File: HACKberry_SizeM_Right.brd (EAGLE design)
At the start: 50.9 x 56.6 mm, 14 parts, among them IC1 OKI-78SR-5_1.5-W36H-C

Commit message: rev1.1
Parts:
- moved U$7 5.24 mm to (44.5, 11.4), turned to 270 degrees
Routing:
- net GND: track 166.2 -> 128.4 mm, vias 0 -> 2
- net SWITCH_HOLD: track 85.2 -> 56.4 mm, vias 3 -> 2
- net +5V: track 59.0 -> 49.9 mm
- net PIN_MIDDLESERVO: track 62.0 -> 69.7 mm, vias 1 -> 2
- net PIN_INDEXSERVO: track 66.4 -> 74.0 mm, vias 3 -> 0
- net V+: track 25.4 -> 32.5 mm, vias 0 -> 1
- net PIN_THUMBSERVO: track 56.9 -> 63.2 mm, vias 3 -> 2
- net N$11: track 58.1 -> 55.2 mm, vias 1 -> 2
- net SWITCH_INIT: track 52.4 -> 53.3 mm, vias 3 -> 2
- net SWITCH_THUMB: track 28.9 -> 29.6 mm, vias 1 -> 2
- net SWITCH_MODE: track 40.5 -> 39.9 mm, vias 3 -> 2
- net N$1: vias 0 -> 1
- added copper zone on layer 1, net GND
- removed copper zone on layer 1, net N$4
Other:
- outline, holes or cut-outs redrawn

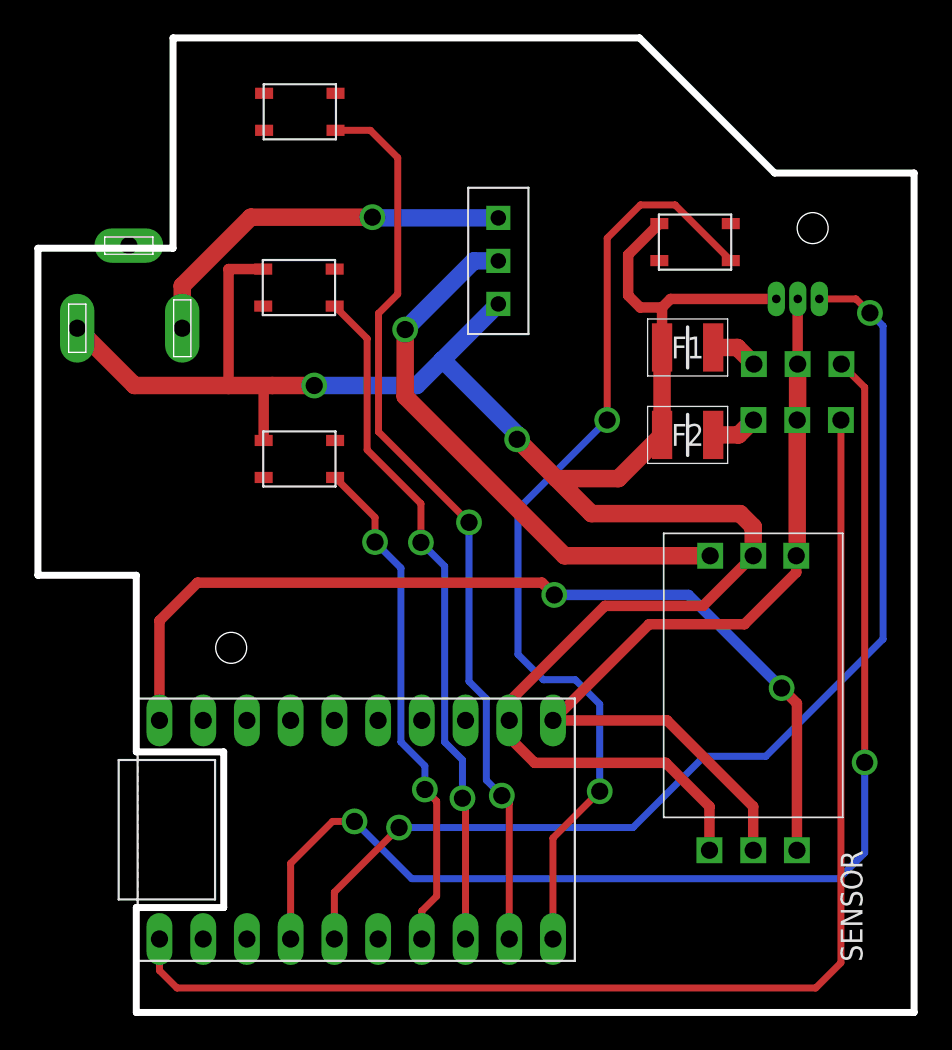
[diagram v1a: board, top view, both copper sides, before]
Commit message: ポリスイッチを取り除き, サーボの電源ラインにパスコンを追加した.
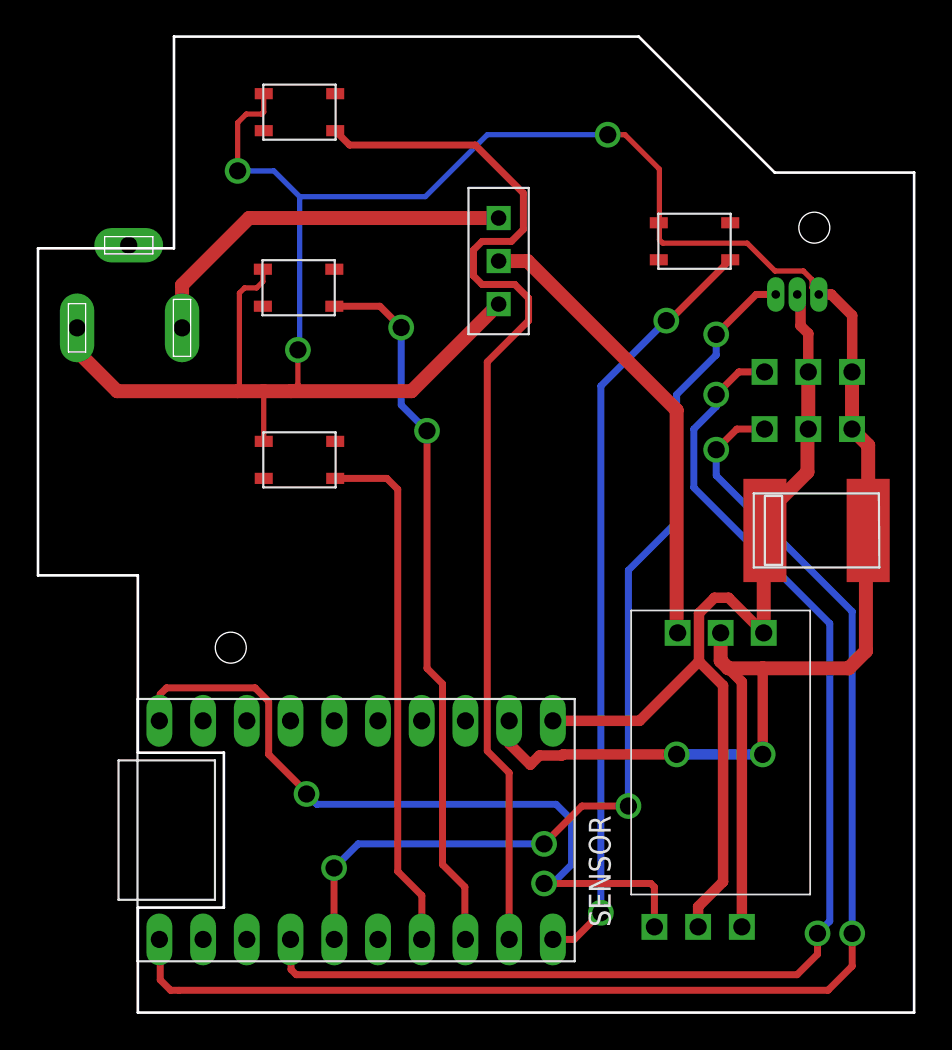
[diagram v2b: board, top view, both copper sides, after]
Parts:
- removed F1, F2: MICROSMD010F-2, HbHandBoard_SizeM:FUSC3226X85N
- added U$8: P-11867_ECASD41C476M040KA0, Akizuki:ECASD41C476M040KA0
- moved U$7 5.48 mm to (41.2, 6.98), turned to 90 degrees
- moved IC1 4.86 mm to (42.6, 17.1)
- moved INDEXPIN 0.83 mm to (47.6, 35.9), turned to 270 degrees
- moved MIDDLEPIN 0.77 mm to (47.6, 39.2), turned to 270 degrees
- moved THUMBPIN 0.26 mm to (47.0, 43.7), turned to 270 degrees
- moved U$5 0.06 mm to (41.0, 46.8)
- moved U$4 0.05 mm to (18.1, 34.1)
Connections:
- removed net N$2: F1.2, MIDDLEPIN.SERVO_GND
- removed net N$3: F2.2, INDEXPIN.SERVO_GND
- net +5V: now also U$8.+
- net GND: now also INDEXPIN.SERVO_GND, MIDDLEPIN.SERVO_GND, U$8.-; no longer F1.1, F2.1
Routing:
- net GND: track 128.4 -> 170.3 mm, vias 2 -> 5
- net SWITCH_HOLD: track 56.4 -> 44.6 mm
- net N$11: track 55.2 -> 44.1 mm
- net SWITCH_INIT: track 53.3 -> 61.9 mm, vias 2 -> 0
- net PIN_THUMBSERVO: track 63.2 -> 56.7 mm, vias 2 -> 4
- net PIN_INDEXSERVO: track 74.0 -> 80.0 mm, vias 0 -> 2
- net V+: track 32.5 -> 26.9 mm, vias 1 -> 0
- net +5V: track 49.9 -> 55.3 mm
- net PIN_MIDDLESERVO: track 69.7 -> 72.9 mm
- net N$2: track 2.77 -> 0.00 mm
- net N$3: track 2.70 -> 0.00 mm
- net SWITCH_MODE: track 39.9 -> 41.5 mm
- net SWITCH_THUMB: track 29.6 -> 30.6 mm, vias 2 -> 0
- net N$1: vias 1 -> 0
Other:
- board size 50.9 x 56.6 mm -> 50.9 x 56.7 mm

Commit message: 8milのDRUに対応
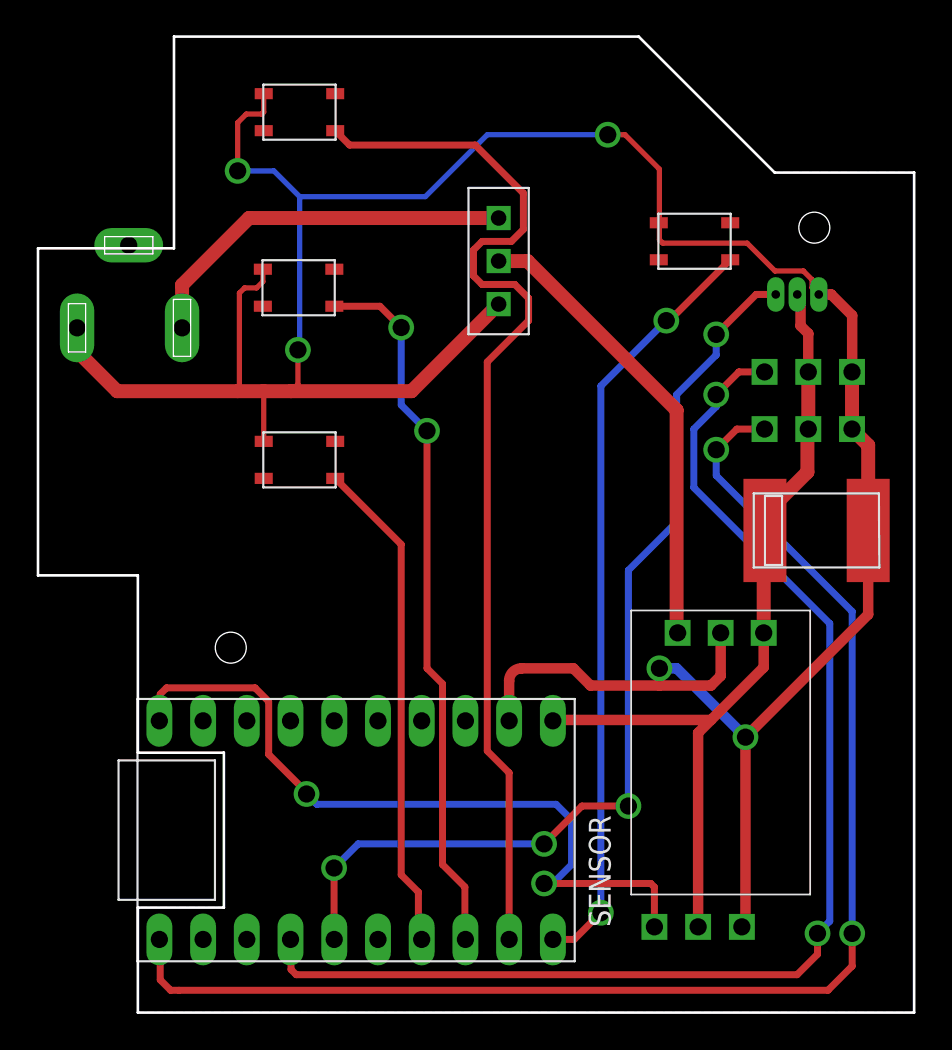
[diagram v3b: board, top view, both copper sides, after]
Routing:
- net +5V: track 55.3 -> 48.9 mm
- net GND: track 170.3 -> 166.6 mm
- net SWITCH_THUMB: track 30.6 -> 28.9 mm
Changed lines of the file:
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@@
 <wire x1="17.6" y1="38.1" x2="24.6" y2="38.1" width="0.8128" layer="1"/>
 <wire x1="24.6" y1="38.1" x2="29.66" y2="43.16" width="0.8128" layer="1"/>
-<wire x1="51.13" y1="30.01" x2="51.13" y2="34.96" width="0.8128" layer="1"/>
+<wire x1="51.13" y1="34.96" x2="51.13" y2="30.01" width="0.8128" layer="1"/>
 <wire x1="51.13" y1="34.96" x2="50.19" y2="35.9" width="0.8128" layer="1"/>
 <wire x1="50.19" y1="39.22" x2="50.19" y2="35.9" width="0.8128" layer="1"/>
-<wire x1="42.56" y1="22.44" x2="42.56" y2="24.06" width="0.8128" layer="1"/>
-<wire x1="42.56" y1="22.44" x2="43" y2="22" width="0.8128" layer="1"/>
-<wire x1="43" y1="22" x2="45" y2="22" width="0.8128" layer="1"/>
-<wire x1="45" y1="22" x2="50" y2="22" width="0.8128" layer="1"/>
-<wire x1="50" y1="22" x2="51" y2="23" width="0.8128" layer="1"/>
-<wire x1="51" y1="23" x2="51" y2="29.88" width="0.8128" layer="1"/>
-<wire x1="51" y1="29.88" x2="51.13" y2="30.01" width="0.8128" layer="1"/>
-<wire x1="43.79" y1="6.98" x2="43.79" y2="21.21" width="0.6096" layer="1"/>
-<wire x1="43.79" y1="21.21" x2="42.56" y2="22.44" width="0.6096" layer="1"/>
-<wire x1="30.27" y1="18.95" x2="30.27" y2="17.63" width="0.6096" layer="1"/>
-<wire x1="31.5" y1="16.4" x2="30.27" y2="17.63" width="0.6096" layer="1"/>
 <wire x1="48.98" y1="43.72" x2="48.26" y2="43.72" width="0.6096" layer="1"/>
 <wire x1="48.98" y1="43.72" x2="50.2" y2="42.5" width="0.6096" layer="1"/>
 <wire x1="50.2" y1="42.5" x2="50.2" y2="39.23" width="0.6096" layer="1"/>
 <wire x1="50.2" y1="39.23" x2="50.19" y2="39.22" width="0.6096" layer="1"/>
-<wire x1="45" y1="22" x2="45" y2="17" width="0.6096" layer="1"/>
-<via x="45" y="17" extent="1-16" drill="1" diameter="1.5" shape="square"/>
-<wire x1="45" y1="17" x2="40" y2="17" width="0.6096" layer="16"/>
-<via x="40" y="17" extent="1-16" drill="1" diameter="1.5" shape="square"/>
-<wire x1="40" y1="17" x2="33.39874375" y2="17" width="0.6096" layer="1"/>
-<wire x1="33.39874375" y1="17" x2="33.33274375" y2="16.934" width="0.6096" layer="1"/>
-<wire x1="32.034" y1="16.934" x2="31.5" y2="16.4" width="0.6096" layer="1"/>
-<wire x1="33.33274375" y1="16.934" x2="32.034" y2="16.934" width="0.6096" layer="1"/>
 <wire x1="16.015" y1="35.185" x2="16.015" y2="38.085" width="0.3048" layer="1"/>
 <wire x1="16.015" y1="38.085" x2="16" y2="38.1" width="0.3048" layer="1"/>
@@
 <vertex x="10.8" y="46.4"/>
 </polygon>
+<wire x1="42.56" y1="24.06" x2="42.56" y2="21.56" width="0.6096" layer="1"/>
+<wire x1="42" y1="21" x2="42.56" y2="21.56" width="0.6096" layer="1"/>
+<wire x1="39" y1="21" x2="42" y2="21" width="0.6096" layer="1"/>
+<wire x1="39" y1="21" x2="35" y2="21" width="0.6096" layer="1"/>
+<wire x1="35" y1="21" x2="34" y2="22" width="0.6096" layer="1"/>
+<wire x1="31" y1="22" x2="30.27" y2="21.27" width="0.6096" layer="1" curve="90"/>
+<wire x1="30.27" y1="21.27" x2="30.27" y2="18.95" width="0.6096" layer="1"/>
+<wire x1="34" y1="22" x2="31" y2="22" width="0.6096" layer="1"/>
+<wire x1="51.13" y1="30.01" x2="51.13" y2="25.13" width="0.6096" layer="1"/>
+<wire x1="51.13" y1="25.13" x2="44" y2="18" width="0.6096" layer="1"/>
+<wire x1="44" y1="18" x2="44" y2="7.19" width="0.6096" layer="1"/>
+<wire x1="44" y1="7.19" x2="43.79" y2="6.98" width="0.6096" layer="1"/>
+<via x="44" y="18" extent="1-16" drill="1" diameter="1.5"/>
+<wire x1="44" y1="18" x2="40" y2="22" width="0.6096" layer="16"/>
+<wire x1="40" y1="22" x2="39" y2="22" width="0.6096" layer="16"/>
+<via x="39" y="22" extent="1-16" drill="1" diameter="1.5"/>
+<wire x1="39" y1="22" x2="39" y2="21" width="0.6096" layer="1"/>
 </signal>
 <signal name="+5V">
@@
 <contactref element="U$6" pad="VIN"/>
 <contactref element="U$7" pad="5V"/>
-<wire x1="45.06" y1="24.06" x2="45.06" y2="29.94" width="0.8128" layer="1"/>
+<wire x1="45.06" y1="29.94" x2="45.06" y2="24.06" width="0.8128" layer="1"/>
 <wire x1="45.06" y1="29.94" x2="45.13" y2="30.01" width="0.8128" layer="1"/>
 <wire x1="45.13" y1="30.01" x2="45.13" y2="30.93" width="0.8128" layer="1"/>
@@
 <wire x1="47.6" y1="35.85" x2="47.65" y2="35.9" width="0.8128" layer="1"/>
 <wire x1="47.65" y1="35.9" x2="47.65" y2="39.22" width="0.8128" layer="1"/>
-<wire x1="32.81" y1="18.95" x2="37.85" y2="18.95" width="0.6096" layer="1"/>
-<wire x1="41.3" y1="22.4" x2="37.85" y2="18.95" width="0.6096" layer="1"/>
-<wire x1="41.3" y1="22.4" x2="41.3" y2="25.2" width="0.6096" layer="1"/>
-<wire x1="41.3" y1="25.2" x2="42.2" y2="26.1" width="0.6096" layer="1"/>
-<wire x1="42.2" y1="26.1" x2="43.02" y2="26.1" width="0.6096" layer="1"/>
-<wire x1="43.02" y1="26.1" x2="45.06" y2="24.06" width="0.6096" layer="1"/>
-<wire x1="41.25" y1="6.98" x2="41.25" y2="8.15" width="0.6096" layer="1"/>
-<wire x1="41.25" y1="8.15" x2="42.7" y2="9.6" width="0.6096" layer="1"/>
-<wire x1="42.7" y1="9.6" x2="42.7" y2="21" width="0.6096" layer="1"/>
-<wire x1="42.7" y1="21" x2="41.3" y2="22.4" width="0.6096" layer="1"/>
 <wire x1="47.65" y1="39.22" x2="47.65" y2="41.45" width="0.6096" layer="1"/>
 <wire x1="47.65" y1="41.45" x2="47.2" y2="41.9" width="0.6096" layer="1"/>
 <wire x1="47.2" y1="41.9" x2="47.2" y2="43.53" width="0.6096" layer="1"/>
 <wire x1="47.2" y1="43.53" x2="47.01" y2="43.72" width="0.6096" layer="1"/>
+<wire x1="45.06" y1="24.06" x2="45.06" y2="22.06" width="0.6096" layer="1"/>
+<wire x1="32.86" y1="19" x2="32.81" y2="18.95" width="0.6096" layer="1" curve="90"/>
+<wire x1="42" y1="19" x2="45.06" y2="22.06" width="0.6096" layer="1"/>
+<wire x1="42" y1="19" x2="32.86" y2="19" width="0.6096" layer="1"/>
+<wire x1="41.25" y1="6.98" x2="41.25" y2="18.25" width="0.6096" layer="1"/>
+<wire x1="41.25" y1="18.25" x2="42" y2="19" width="0.6096" layer="1"/>
 </signal>
 <signal name="SWITCH_INIT">
@@
 <contactref element="U$4" pad="PINB_RIGHT"/>
 <contactref element="U$6" pad="GPIO_3"/>
-<wire x1="20.165" y1="33.035" x2="23.165" y2="33.035" width="0.4064" layer="1"/>
-<wire x1="23.165" y1="33.035" x2="23.8" y2="32.4" width="0.4064" layer="1"/>
-<wire x1="23.8" y1="32.4" x2="23.8" y2="10.2" width="0.4064" layer="1"/>
-<wire x1="23.8" y1="10.2" x2="25.2" y2="8.8" width="0.4064" layer="1"/>
-<wire x1="25.2" y1="8.8" x2="25.2" y2="6.26" width="0.4064" layer="1"/>
-<wire x1="25.2" y1="6.26" x2="25.19" y2="6.25" width="0.4064" layer="1"/>
+<wire x1="20.165" y1="33.035" x2="24" y2="29.2" width="0.4064" layer="1"/>
+<wire x1="24" y1="10" x2="25" y2="9" width="0.4064" layer="1"/>
+<wire x1="25" y1="9" x2="25" y2="6.44" width="0.4064" layer="1"/>
+<wire x1="25" y1="6.44" x2="25.19" y2="6.25" width="0.4064" layer="1"/>
+<wire x1="24" y1="29.2" x2="24" y2="10" width="0.4064" layer="1"/>
 </signal>
 <signal name="SWITCH_HOLD">
@@
 </signal>
 </signals>
+<errors>
+</errors>
 </board>
 </drawing>
